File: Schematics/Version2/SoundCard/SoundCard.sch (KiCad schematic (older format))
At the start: 12 parts, among them J1 Screw_Terminal_01x03, J2 AudioJack3, U1 TL072

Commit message: Update the footprint for the 3.5mm jack.
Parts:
- J2: footprint Connector_Audio:Jack_3.5mm_CUI_SJ1-3533NG_Horizontal -> Connector_Audio:Jack_3.5mm_CUI_SJ1-3523N
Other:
- note removed: "TODO: Need the proper footprint for the audio jack."
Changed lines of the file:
@@
 F 0 "J2" H 7170 5133 50  0000 R CNN
 F 1 "AudioJack3" H 7170 5224 50  0000 R CNN
-F 2 "Connector_Audio:Jack_3.5mm_CUI_SJ1-3533NG_Horizontal" H 7450 5200 50  0001 C CNN
+F 2 "Connector_Audio:Jack_3.5mm_CUI_SJ1-3523N" H 7450 5200 50  0001 C CNN
 F 3 "~" H 7450 5200 50  0001 C CNN
 	1    7450 5200
@@
 	7250 5100 7150 5100
 Connection ~ 6750 5100
-Text Notes 7350 4900 0    50   ~ 0
-TODO: Need the proper footprint for the audio jack.
 Wire Wire Line
 	3000 1750 3150 1750

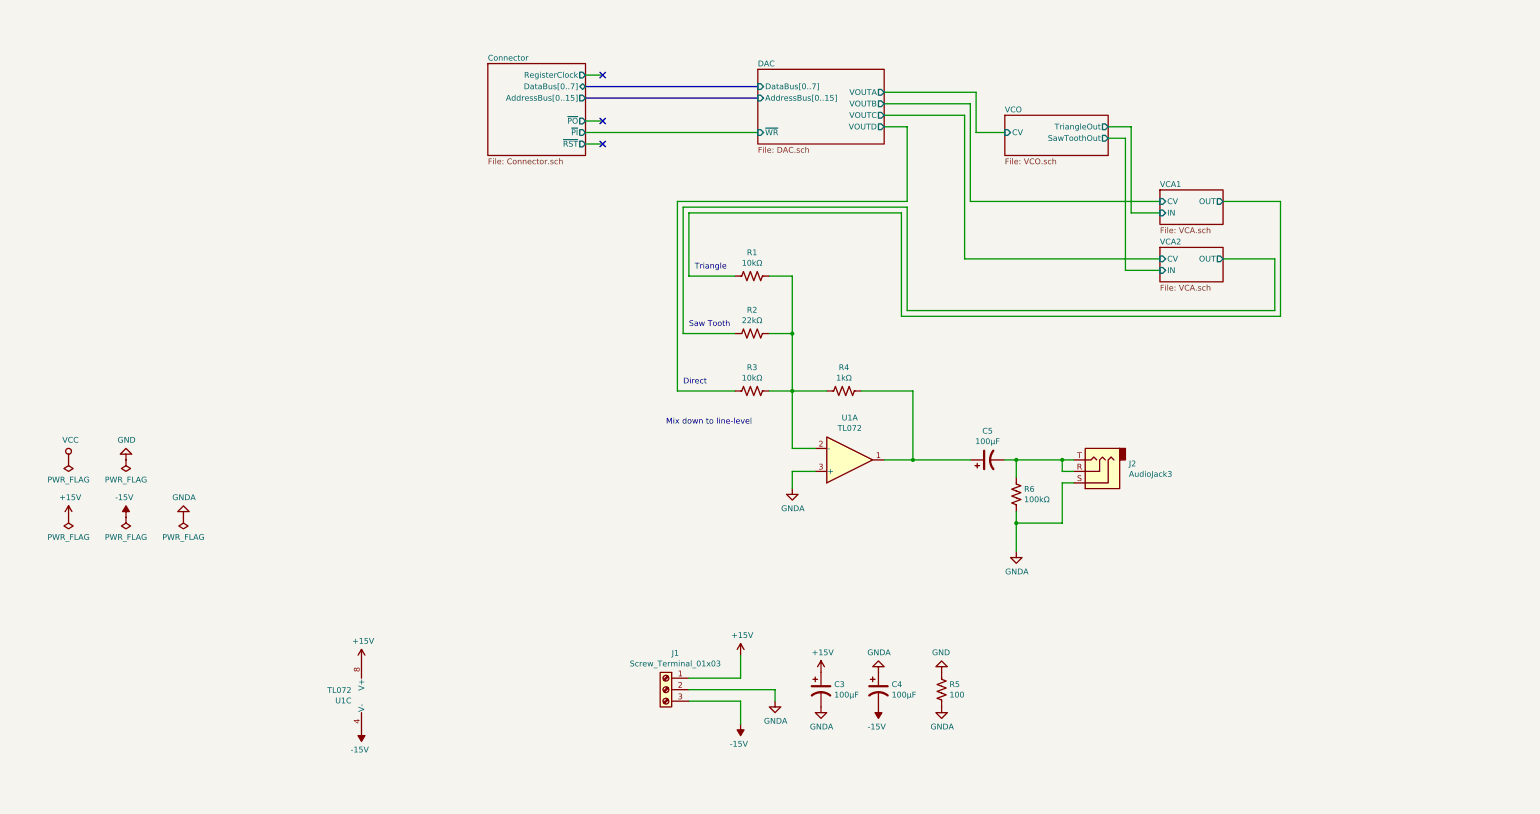
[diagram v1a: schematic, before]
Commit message: Sound card: revise circuit schematic to include second oscillator, VCA
The AS3360 VCA is a more effective and compact amplifier than the JFET
based design in the previous revision.
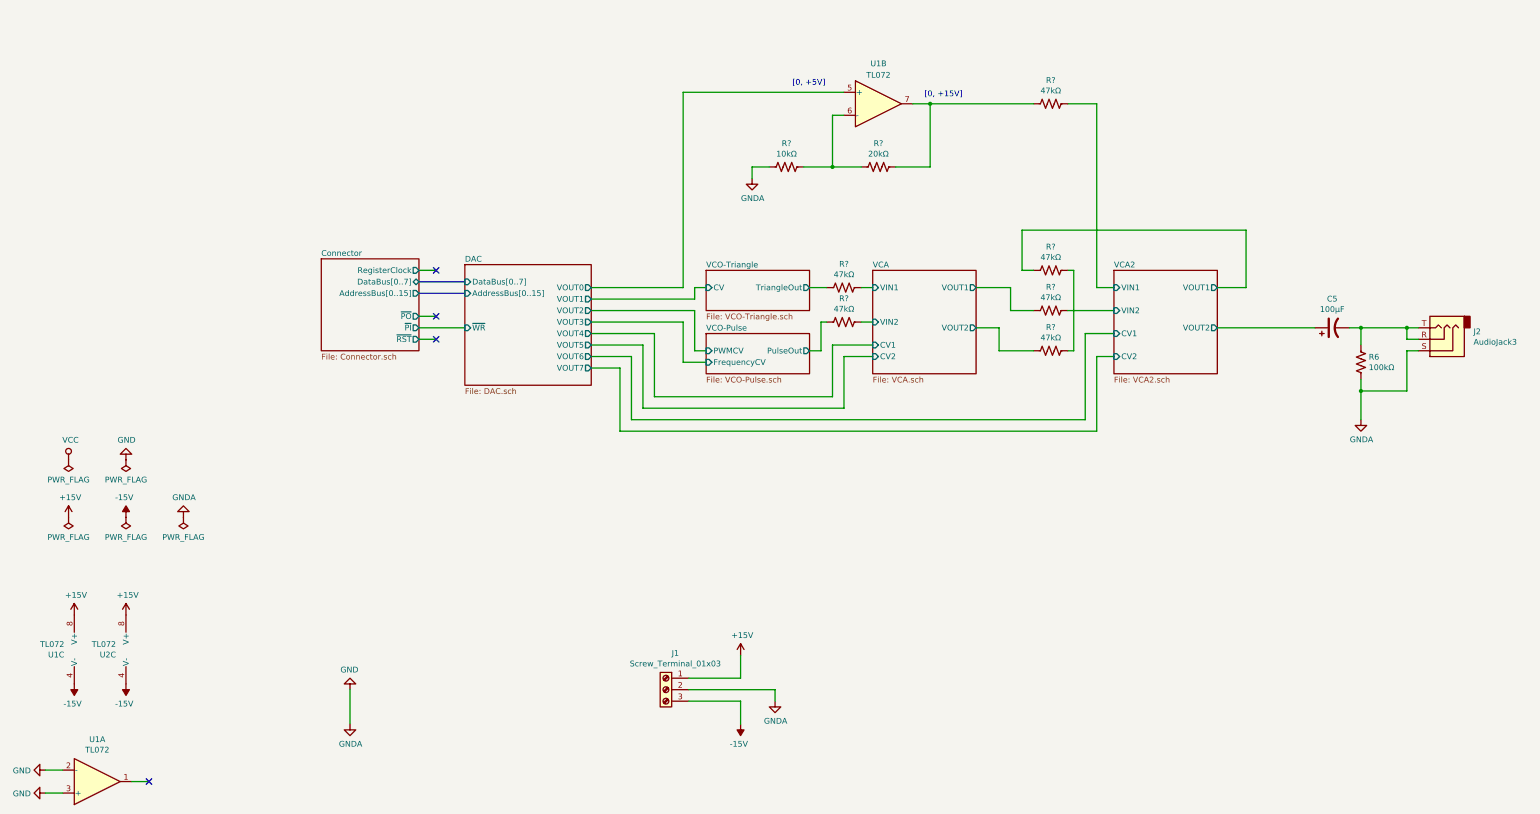
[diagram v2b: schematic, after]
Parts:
- removed C3, C4: 100µF, Capacitor_THT:CP_Radial_D6.3mm_P2.50mm, symbol Device:CP1
- removed R1, R3: 10kΩ, Resistor_THT:R_Axial_DIN0207_L6.3mm_D2.5mm_P7.62mm_Horizontal, symbol Device:R_US
- removed R2: 22kΩ, Resistor_THT:R_Axial_DIN0207_L6.3mm_D2.5mm_P7.62mm_Horizontal, symbol Device:R_US
- removed R4: 1kΩ, Resistor_THT:R_Axial_DIN0207_L6.3mm_D2.5mm_P7.62mm_Horizontal, symbol Device:R_US
- removed R5: 100, Resistor_THT:R_Axial_DIN0207_L6.3mm_D2.5mm_P7.62mm_Horizontal, symbol Device:R_US
- added R? (x6): 47kΩ, symbol Device:R_US
- added R?: 10kΩ, Resistor_THT:R_Axial_DIN0207_L6.3mm_D2.5mm_P7.62mm_Horizontal, symbol Device:R_US
- added R?: 20kΩ, Resistor_THT:R_Axial_DIN0207_L6.3mm_D2.5mm_P7.62mm_Horizontal, symbol Device:R_US
- added unit 2 of U1
- added U2: TL072, Package_DIP:DIP-8_W7.62mm_Socket, symbol Amplifier_Operational:TL072
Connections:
- net GNDA is gone; now on net GND: J1.2 (Pin_2), J2.S, R6.2, U1.3 (+)
- net +15V: now also U2.8 (V+)
- net -15V: now also U2.4 (V-)
- net GND: now also U1.2 (-), R?.1
- net at U1.1: no longer C5.1
- new net: R?.2, R?.2, U1.7
- new net: R?.1, R?.1
- new net: R?.1, R?.2, U1.6 (-)
- new net DAC/VOUT0: U1.5 (+)
- new net VCA/VIN1: R?.1
- new net VCA/VIN2: R?.1
- new net VCA/VOUT1: R?.2
- new net VCA/VOUT2: R?.2
- new net VCA2/VIN1: R?.1
- new net VCA2/VIN2: R?.1
- new net VCA2/VOUT1: R?.2
- new net VCA2/VOUT2: C5.1
- new net VCO-Pulse/PulseOut: R?.2
- new net VCO-Triangle/TriangleOut: R?.2
- no-connect marks 3 -> 4
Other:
- note added: "[0, +15V]"
- note added: "[0, +5V]"
- note removed: "Direct"
- note removed: "Mix down to line-level"
- note removed: "Saw Tooth"
- note removed: "Triangle"
- moved on the sheet: C5, J2, R6, U1A, U1C

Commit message: Sound card: Start assigning SMD footprints to schematic components.
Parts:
- U1, U2: footprint Package_DIP:DIP-8_W7.62mm_Socket -> Package_SO:SOIC-8_3.9x4.9mm_P1.27mm
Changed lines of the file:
@@
 F 0 "U1" H -1250 7533 50  0000 C CNN
 F 1 "TL072" H -1250 7624 50  0000 C CNN
-F 2 "Package_DIP:DIP-8_W7.62mm_Socket" H -1250 7900 50  0001 C CNN
+F 2 "Package_SO:SOIC-8_3.9x4.9mm_P1.27mm" H -1250 7900 50  0001 C CNN
 F 3 "http://www.ti.com/lit/ds/symlink/tl071.pdf" H -1250 7900 50  0001 C CNN
 	1    -1250 7900
@@
 F 0 "U1" H -1537 6704 50  0000 R CNN
 F 1 "TL072" H -1537 6795 50  0000 R CNN
-F 2 "Package_DIP:DIP-8_W7.62mm_Socket" H -1350 6750 50  0001 C CNN
+F 2 "Package_SO:SOIC-8_3.9x4.9mm_P1.27mm" H -1350 6750 50  0001 C CNN
 F 3 "http://www.ti.com/lit/ds/symlink/tl071.pdf" H -1350 6750 50  0001 C CNN
 	3    -1350 6750
@@
 F 0 "U1" H 5550 2350 50  0000 C CNN
 F 1 "TL072" H 5550 2250 50  0000 C CNN
-F 2 "Package_DIP:DIP-8_W7.62mm_Socket" H 5550 2000 50  0001 C CNN
+F 2 "Package_SO:SOIC-8_3.9x4.9mm_P1.27mm" H 5550 2000 50  0001 C CNN
 F 3 "http://www.ti.com/lit/ds/symlink/tl071.pdf" H 5550 2000 50  0001 C CNN
 	2    5550 2000
@@
 F 0 "U2" H -1087 6704 50  0000 R CNN
 F 1 "TL072" H -1087 6795 50  0000 R CNN
-F 2 "Package_DIP:DIP-8_W7.62mm_Socket" H -900 6750 50  0001 C CNN
+F 2 "Package_SO:SOIC-8_3.9x4.9mm_P1.27mm" H -900 6750 50  0001 C CNN
 F 3 "http://www.ti.com/lit/ds/symlink/tl071.pdf" H -900 6750 50  0001 C CNN
 	3    -900 6750

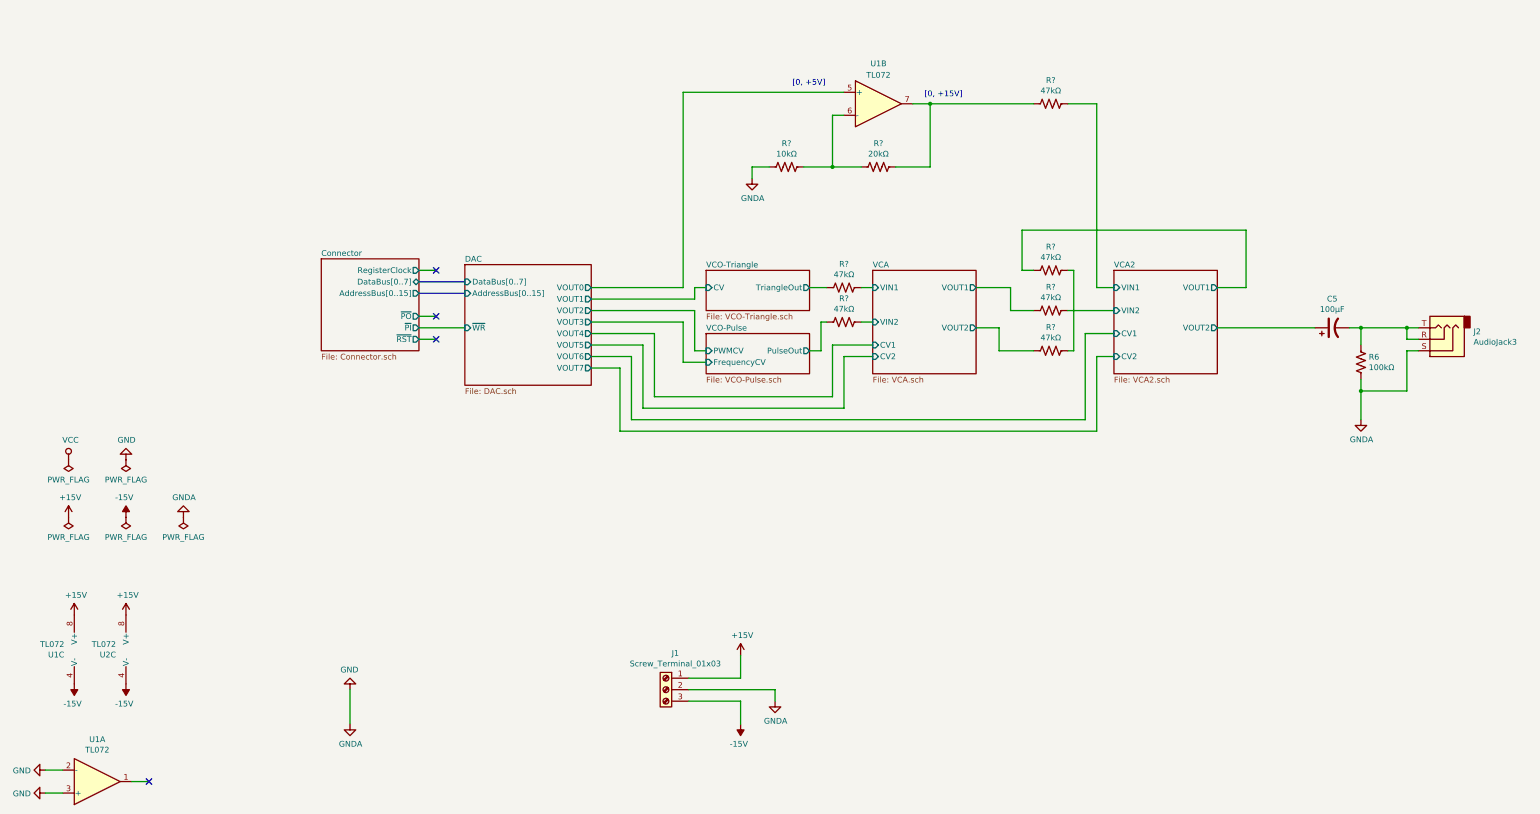
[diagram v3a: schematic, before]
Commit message: Sound card: add the Electric Druid Noise 1B digital sound generator.
The gain on the noise voice is controlled by one of the AS3360 units.
The master gain control is removed in order to make this possible.
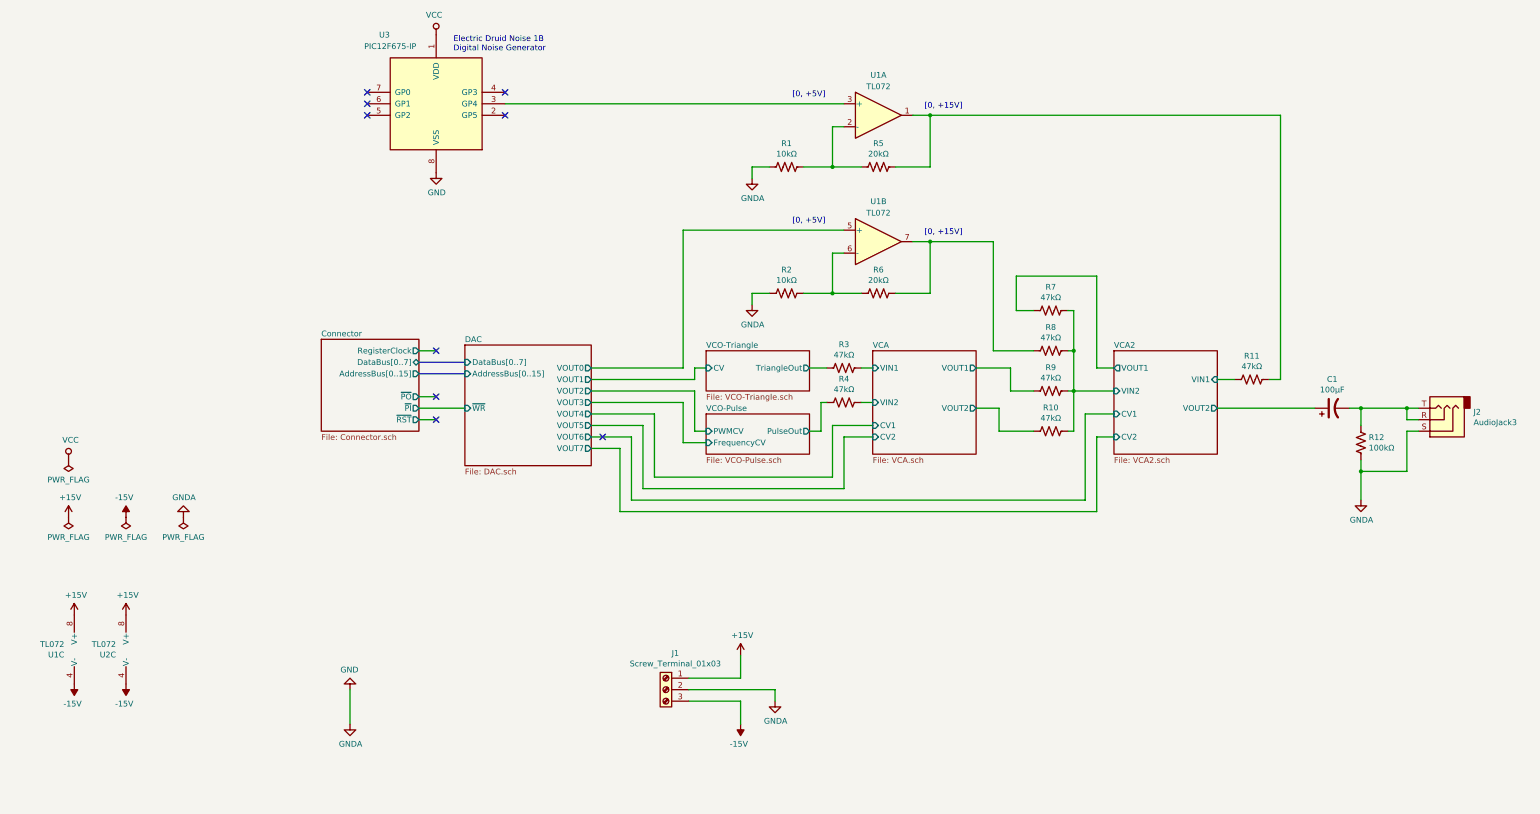
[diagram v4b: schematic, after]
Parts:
- added R1: 10kΩ, Resistor_THT:R_Axial_DIN0207_L6.3mm_D2.5mm_P7.62mm_Horizontal, symbol Device:R_US
- added R11: 47kΩ, symbol Device:R_US
- added R5: 20kΩ, Resistor_THT:R_Axial_DIN0207_L6.3mm_D2.5mm_P7.62mm_Horizontal, symbol Device:R_US
- added U3: PIC12F675-IP, Package_DIP:DIP-8_W7.62mm_Socket, symbol MCU_Microchip_PIC12:PIC12F675-IP
- gave numbers to parts that had none: 8
- renumbered C5 to C1, R6 to R12
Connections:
- net GND: now also R1.1, U3.8 (VSS); no longer U1.2 (-), U1.3 (+)
- net VCA2/VIN1: now also R11.2; no longer R7.1
- net VCA2/VIN2: now also R10.1, R7.1, R8.1
- net VCA2/VOUT1: now also R7.2; no longer R8.2
- net VCC: now also U3.1 (VDD)
- net at U1.1: now also R11.1, R5.2
- net at R6.2, U1.7: now also R8.2; no longer R7.2
- new net: U1.3 (+), U3.3 (GP4)
- new net: R1.2, R5.1, U1.2 (-)
- no-connect marks 4 -> 9
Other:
- note added: "Electric Druid Noise 1B\nDigital Noise Generator"
- moved on the sheet: C1, J2, R10, R12, R2, R3, R4, R6, R7, R8, R9, U1B

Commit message: Sound Card: Finish routing SMD PCB for rev 2
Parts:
- added C11, C12: 100µF, Capacitor_SMD:C_1206_3216Metric_Pad1.42x1.75mm_HandSolder, symbol Device:CP1
- C1: footprint Capacitor_THT:CP_Radial_D6.3mm_P2.50mm -> Capacitor_SMD:C_1206_3216Metric_Pad1.42x1.75mm_HandSolder
- R1, R12, R2, R5, R6: footprint Resistor_THT:R_Axial_DIN0207_L6.3mm_D2.5mm_P7.62mm_Horizontal -> Resistor_SMD:R_0603_1608Metric_Pad1.05x0.95mm_HandSolder
- R10, R11, R3, R4, R7, R8, R9: footprint (none) -> Resistor_SMD:R_0603_1608Metric_Pad1.05x0.95mm_HandSolder
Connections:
- net +15V: now also C11.1
- net -15V: now also C12.2
- net GND: now also C11.2, C12.1
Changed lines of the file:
@@
 F 0 "R12" H 9818 4996 50  0000 L CNN
 F 1 "100kΩ" H 9818 4905 50  0000 L CNN
-F 2 "Resistor_THT:R_Axial_DIN0207_L6.3mm_D2.5mm_P7.62mm_Horizontal" V 9790 4940 50  0001 C CNN
+F 2 "Resistor_SMD:R_0603_1608Metric_Pad1.05x0.95mm_HandSolder" V 9790 4940 50  0001 C CNN
 F 3 "~" H 9750 4950 50  0001 C CNN
 	1    9750 4950
@@
 F 0 "C1" V 9752 4650 50  0000 C CNN
 F 1 "100µF" V 9661 4650 50  0000 C CNN
-F 2 "Capacitor_THT:CP_Radial_D6.3mm_P2.50mm" H 9500 4650 50  0001 C CNN
+F 2 "Capacitor_SMD:C_1206_3216Metric_Pad1.42x1.75mm_HandSolder" H 9500 4650 50  0001 C CNN
 F 3 "~" H 9500 4650 50  0001 C CNN
 	1    9500 4650
@@
 F 0 "R3" V 5045 4300 50  0000 C CNN
 F 1 "47kΩ" V 5136 4300 50  0000 C CNN
-F 2 "" V 5290 4290 50  0001 C CNN
+F 2 "Resistor_SMD:R_0603_1608Metric_Pad1.05x0.95mm_HandSolder" V 5290 4290 50  0001 C CNN
 F 3 "~" H 5250 4300 50  0001 C CNN
 	1    5250 4300
@@
 F 0 "R4" V 5045 4600 50  0000 C CNN
 F 1 "47kΩ" V 5136 4600 50  0000 C CNN
-F 2 "" V 5290 4590 50  0001 C CNN
+F 2 "Resistor_SMD:R_0603_1608Metric_Pad1.05x0.95mm_HandSolder" V 5290 4590 50  0001 C CNN
 F 3 "~" H 5250 4600 50  0001 C CNN
 	1    5250 4600
@@
 F 0 "R7" V 6845 3800 50  0000 C CNN
 F 1 "47kΩ" V 6936 3800 50  0000 C CNN
-F 2 "" V 7090 3790 50  0001 C CNN
+F 2 "Resistor_SMD:R_0603_1608Metric_Pad1.05x0.95mm_HandSolder" V 7090 3790 50  0001 C CNN
 F 3 "~" H 7050 3800 50  0001 C CNN
 	1    7050 3800
@@
 F 0 "R9" V 6845 4500 50  0000 C CNN
 F 1 "47kΩ" V 6936 4500 50  0000 C CNN
-F 2 "" V 7090 4490 50  0001 C CNN
+F 2 "Resistor_SMD:R_0603_1608Metric_Pad1.05x0.95mm_HandSolder" V 7090 4490 50  0001 C CNN
 F 3 "~" H 7050 4500 50  0001 C CNN
 	1    7050 4500
@@
 F 0 "R10" V 6845 4850 50  0000 C CNN
 F 1 "47kΩ" V 6936 4850 50  0000 C CNN
-F 2 "" V 7090 4840 50  0001 C CNN
+F 2 "Resistor_SMD:R_0603_1608Metric_Pad1.05x0.95mm_HandSolder" V 7090 4840 50  0001 C CNN
 F 3 "~" H 7050 4850 50  0001 C CNN
 	1    7050 4850
@@
 F 0 "R2" V 4955 3650 50  0000 C CNN
 F 1 "10kΩ" V 4864 3650 50  0000 C CNN
-F 2 "Resistor_THT:R_Axial_DIN0207_L6.3mm_D2.5mm_P7.62mm_Horizontal" V 4790 3640 50  0001 C CNN
+F 2 "Resistor_SMD:R_0603_1608Metric_Pad1.05x0.95mm_HandSolder" V 4790 3640 50  0001 C CNN
 F 3 "~" H 4750 3650 50  0001 C CNN
 	1    4750 3650
@@
 F 0 "R6" V 5755 3650 50  0000 C CNN
 F 1 "20kΩ" V 5664 3650 50  0000 C CNN
-F 2 "Resistor_THT:R_Axial_DIN0207_L6.3mm_D2.5mm_P7.62mm_Horizontal" V 5590 3640 50  0001 C CNN
+F 2 "Resistor_SMD:R_0603_1608Metric_Pad1.05x0.95mm_HandSolder" V 5590 3640 50  0001 C CNN
 F 3 "~" H 5550 3650 50  0001 C CNN
 	1    5550 3650
@@
 F 0 "R8" V 6845 4150 50  0000 C CNN
 F 1 "47kΩ" V 6936 4150 50  0000 C CNN
-F 2 "" V 7090 4140 50  0001 C CNN
+F 2 "Resistor_SMD:R_0603_1608Metric_Pad1.05x0.95mm_HandSolder" V 7090 4140 50  0001 C CNN
 F 3 "~" H 7050 4150 50  0001 C CNN
 	1    7050 4150
@@
 F 0 "R1" V 4955 2550 50  0000 C CNN
 F 1 "10kΩ" V 4864 2550 50  0000 C CNN
-F 2 "Resistor_THT:R_Axial_DIN0207_L6.3mm_D2.5mm_P7.62mm_Horizontal" V 4790 2540 50  0001 C CNN
+F 2 "Resistor_SMD:R_0603_1608Metric_Pad1.05x0.95mm_HandSolder" V 4790 2540 50  0001 C CNN
 F 3 "~" H 4750 2550 50  0001 C CNN
 	1    4750 2550
@@
 F 0 "R5" V 5755 2550 50  0000 C CNN
 F 1 "20kΩ" V 5664 2550 50  0000 C CNN
-F 2 "Resistor_THT:R_Axial_DIN0207_L6.3mm_D2.5mm_P7.62mm_Horizontal" V 5590 2540 50  0001 C CNN
+F 2 "Resistor_SMD:R_0603_1608Metric_Pad1.05x0.95mm_HandSolder" V 5590 2540 50  0001 C CNN
 F 3 "~" H 5550 2550 50  0001 C CNN
 	1    5550 2550
@@
 F 0 "R11" V 8595 4400 50  0000 C CNN
 F 1 "47kΩ" V 8686 4400 50  0000 C CNN
-F 2 "" V 8840 4390 50  0001 C CNN
+F 2 "Resistor_SMD:R_0603_1608Metric_Pad1.05x0.95mm_HandSolder" V 8840 4390 50  0001 C CNN
 F 3 "~" H 8800 4400 50  0001 C CNN
 	1    8800 4400
@@
 	7250 4500 7250 4850
 NoConn ~ 3150 4900
+$Comp
+L Device:CP1 C11
+U 1 1 5F179E25
+P 5600 6700
+F 0 "C11" H 5850 6750 50  0000 C CNN
+F 1 "100µF" H 5850 6650 50  0000 C CNN
+F 2 "Capacitor_SMD:C_1206_3216Metric_Pad1.42x1.75mm_HandSolder" H 5600 6700 50  0001 C CNN
+F 3 "~" H 5600 6700 50  0001 C CNN
+	1    5600 6700
+	1    0    0    -1
+$EndComp
+$Comp
+L power:+15V #PWR05
+U 1 1 5F17ACBF
+P 5600 6550
+F 0 "#PWR05" H 5600 6400 50  0001 C CNN
+F 1 "+15V" H 5615 6723 50  0000 C CNN
+F 2 "" H 5600 6550 50  0001 C CNN
+F 3 "" H 5600 6550 50  0001 C CNN
+	1    5600 6550
+	1    0    0    -1
+$EndComp
+$Comp
+L power:GNDA #PWR089
+U 1 1 5F17B22C
+P 5600 6850
+F 0 "#PWR089" H 5600 6600 50  0001 C CNN
+F 1 "GNDA" H 5605 6677 50  0000 C CNN
+F 2 "" H 5600 6850 50  0001 C CNN
+F 3 "" H 5600 6850 50  0001 C CNN
+	1    5600 6850
+	1    0    0    -1
+$EndComp
+$Comp
+L Device:CP1 C12
+U 1 1 5F17C51E
+P 6200 6700
+F 0 "C12" H 6450 6750 50  0000 C CNN
+F 1 "100µF" H 6450 6650 50  0000 C CNN
+F 2 "Capacitor_SMD:C_1206_3216Metric_Pad1.42x1.75mm_HandSolder" H 6200 6700 50  0001 C CNN
+F 3 "~" H 6200 6700 50  0001 C CNN
+	1    6200 6700
+	1    0    0    -1
+$EndComp
+$Comp
+L power:GNDA #PWR090
+U 1 1 5F17C52A
+P 6200 6550
+F 0 "#PWR090" H 6200 6300 50  0001 C CNN
+F 1 "GNDA" H 6205 6377 50  0000 C CNN
+F 2 "" H 6200 6550 50  0001 C CNN
+F 3 "" H 6200 6550 50  0001 C CNN
+	1    6200 6550
+	-1   0    0    1
+$EndComp
+$Comp
+L power:-15V #PWR091
+U 1 1 5F18107B
+P 6200 6850
+F 0 "#PWR091" H 6200 6950 50  0001 C CNN
+F 1 "-15V" H 6215 7023 50  0000 C CNN
+F 2 "" H 6200 6850 50  0001 C CNN
+F 3 "" H 6200 6850 50  0001 C CNN
+	1    6200 6850
+	-1   0    0    1
+$EndComp
 $EndSCHEMATC
